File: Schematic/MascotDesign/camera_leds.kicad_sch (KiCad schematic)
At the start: 11 parts, among them Q1 IRF540N

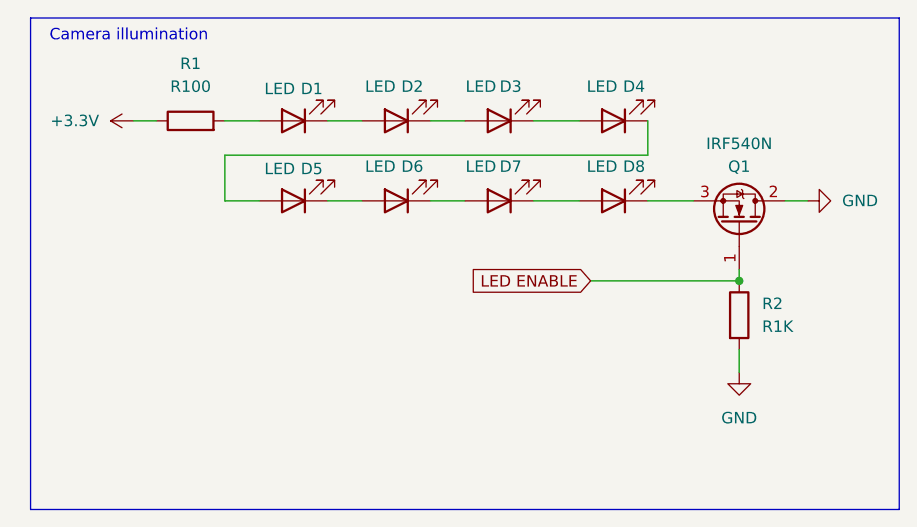
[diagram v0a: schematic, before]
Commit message: Assign footprints and begin PCB layout
Need to check the ECE shop to see what parts we have on hand before we get too far into this, but still.
It's a start.
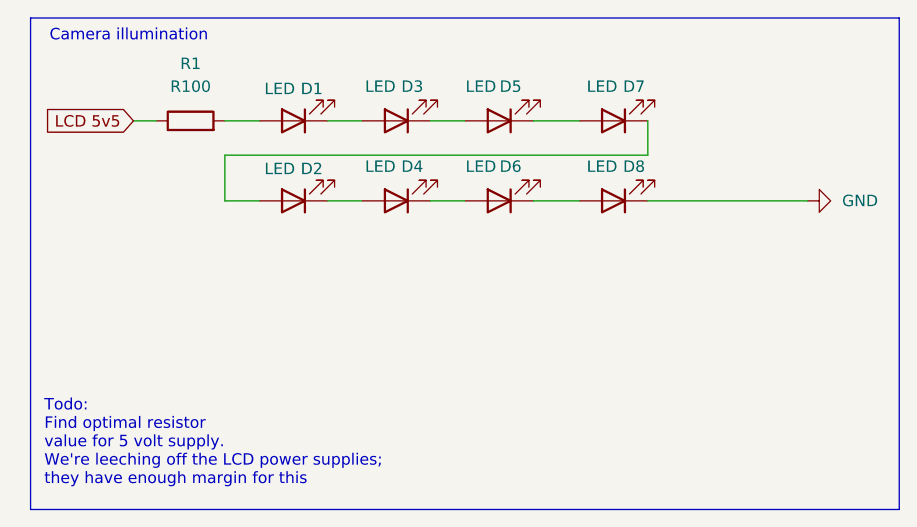
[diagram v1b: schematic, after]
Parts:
- removed Q1: IRF540N, Package_TO_SOT_THT:TO-220-3_Vertical, symbol Transistor_FET:IRF540N
- removed R2: R1K, symbol Device:R
- D1, D8: footprint (none) -> LED_THT:LED_D3.0mm
- D2: renamed from D5; footprint (none) -> LED_THT:LED_D3.0mm
- D3: renamed from D2; footprint (none) -> LED_THT:LED_D3.0mm
- D4: renamed from D6; footprint (none) -> LED_THT:LED_D3.0mm
- D5: renamed from D3; footprint (none) -> LED_THT:LED_D3.0mm
- D6: renamed from D7; footprint (none) -> LED_THT:LED_D3.0mm
- D7: renamed from D4; footprint (none) -> LED_THT:LED_D3.0mm
- R1: footprint (none) -> Resistor_THT:R_Axial_DIN0207_L6.3mm_D2.5mm_P7.62mm_Horizontal
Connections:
- net GND: now also D8.1 (K)
- net +3.3V renamed LCD 5v5
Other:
- note added: "Todo: Find optimal resistor value for 5 volt supply. We're leeching off the LCD power supplies; they have enough margin for this"
- title: (none) -> Camera Light subsystem

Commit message: Work on CAD and schematics
Got most of the components modeled for reference, now arranging them and creating brackets
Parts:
- added J7: LED Connector, Connector_PinHeader_2.54mm:PinHeader_1x02_P2.54mm_Vertical, symbol Connector_Generic:Conn_01x02
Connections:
- net GND: now also J7.2 (Pin_2)
- net LCD 5v5: now also J7.1 (Pin_1)
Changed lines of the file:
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@@
+	(wire
+		(pts
+			(xy 38.1 48.26) (xy 34.29 48.26)
+		)
+		(stroke
+			(width 0)
+			(type default)
+		)
+	)
 	(wire
 		(pts
 			(xy 31.75 27.94) (xy 34.29 27.94)
+		)
+		(stroke
+			(width 0)
+			(type default)
+		)
+	)
+	(wire
+		(pts
+			(xy 38.1 50.8) (xy 34.29 50.8)
 		)
 		(stroke
@@
 		)
 	)
+	(global_label "LCD 5v5"
+		(shape input)
+		(at 34.29 48.26 180)
+		(fields_autoplaced yes)
+		(effects
+			(font
+				(size 1.27 1.27)
+			)
+			(justify right)
+		)
+		(property "Intersheetrefs" "${INTERSHEET_REFS}"
+			(at 23.3825 48.26 0)
+			(effects
+				(font
+					(size 1.27 1.27)
+				)
+				(justify right)
+				(hide yes)
+			)
+		)
+	)
 	(symbol
 		(lib_id "Device:LED")
@@
 	(symbol
 		(lib_id "power:GND")
+		(at 34.29 50.8 270)
+		(unit 1)
+		(exclude_from_sim no)
+		(in_bom yes)
+		(on_board yes)
+		(dnp no)
+		(fields_autoplaced yes)
+		(property "Reference" "#PWR01"
+			(at 27.94 50.8 0)
+			(effects
+				(font
+					(size 1.27 1.27)
+				)
+				(hide yes)
+			)
+		)
+		(property "Value" "GND"
+			(at 30.48 50.7999 90)
+			(effects
+				(font
+					(size 1.27 1.27)
+				)
+				(justify right)
+			)
+		)
+		(property "Footprint" ""
+			(at 34.29 50.8 0)
+			(effects
+				(font
+					(size 1.27 1.27)
+				)
+				(hide yes)
+			)
+		)
+		(property "Datasheet" ""
+			(at 34.29 50.8 0)
+			(effects
+				(font
+					(size 1.27 1.27)
+				)
+				(hide yes)
+			)
+		)
+		(property "Description" "Power symbol creates a global label with name \"GND\" , ground"
+			(at 34.29 50.8 0)
+			(effects
+				(font
+					(size 1.27 1.27)
+				)
+				(hide yes)
+			)
+		)
+		(pin "1"
+		)
+		(instances
+			(project "MascotDesign"
+				(path "/ba045f6c-d730-41b1-992e-d77c9aee61c5/8b76e1c7-16fb-41f9-a46d-90890acff3e2"
+					(reference "#PWR01")
+					(unit 1)
+				)
+			)
+		)
+	)
+	(symbol
+		(lib_id "power:GND")
 		(at 106.68 36.83 90)
 		(unit 1)
@@
 					(unit 1)
 				)
+			)
+		)
+	)
+	(symbol
+		(lib_id "Connector_Generic:Conn_01x02")
+		(at 43.18 48.26 0)
+		(unit 1)
+		(exclude_from_sim no)
+		(in_bom yes)
+		(on_board yes)
+		(dnp no)
+		(property "Reference" "J7"
+			(at 43.18 43.434 0)
+			(effects
+				(font
+					(size 1.27 1.27)
+				)
+				(justify right)
+			)
+		)
+		(property "Value" "LED Connector"
+			(at 43.18 45.212 0)
+			(effects
+				(font
+					(size 1.27 1.27)
+				)
+				(justify right)
+			)
+		)
+		(property "Footprint" "Connector_PinHeader_2.54mm:PinHeader_1x02_P2.54mm_Vertical"
+			(at 43.18 48.26 0)
+			(effects
+				(font
+					(size 1.27 1.27)
+				)
+				(hide yes)
+			)
+		)
+		(property "Datasheet" "~"
+			(at 43.18 48.26 0)
+			(effects
+				(font
+					(size 1.27 1.27)
+				)
+				(hide yes)
+			)
+		)
+		(property "Description" "Generic connector, single row, 01x02, script generated (kicad-library-utils/schlib/autogen/connector/)"
+			(at 43.18 48.26 0)
+			(effects
+				(font
+					(size 1.27 1.27)
+				)
+				(hide yes)
+			)
+		)
+		(pin "2"
+		)
+		(pin "1"
+		)
+		(instances
+			(project "MascotDesign"
+				(path "/ba045f6c-d730-41b1-992e-d77c9aee61c5/8b76e1c7-16fb-41f9-a46d-90890acff3e2"
+					(reference "J7")
+					(unit 1)
+				)

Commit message: Do PCB layout
I need to check our cap footprints to make sure we got the right ones.
Other than that, the PCB should be mostly routed.
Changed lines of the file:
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@@
 		)
+	)
+	(junction
+		(at 36.83 50.8)
+		(diameter 0)
+		(color 0 0 0 0)
 	)
 	(wire
@@
 	(wire
 		(pts
-			(xy 38.1 50.8) (xy 34.29 50.8)
+			(xy 38.1 50.8) (xy 36.83 50.8)
 		)
 		(stroke
@@
 		(pts
 			(xy 76.2 27.94) (xy 81.28 27.94)
+		)
+		(stroke
+			(width 0)
+			(type default)
+		)
+	)
+	(wire
+		(pts
+			(xy 36.83 50.8) (xy 34.29 50.8)
 		)
 		(stroke
@@
 					(unit 1)
 				)
+			)
+		)
+	)
+	(symbol
+		(lib_id "power:PWR_FLAG")
+		(at 36.83 50.8 180)
+		(unit 1)
+		(exclude_from_sim no)
+		(in_bom yes)
+		(on_board yes)
+		(dnp no)
+		(property "Reference" "#FLG04"
+			(at 36.83 52.705 0)
+			(effects
+				(font
+					(size 1.27 1.27)
+				)
+				(hide yes)
+			)
+		)
+		(property "Value" "PWR_FLAG"
+			(at 32.766 55.372 0)
+			(effects
+				(font
+					(size 1.27 1.27)
+				)
+			)
+		)
+		(property "Footprint" ""
+			(at 36.83 50.8 0)
+			(effects
+				(font
+					(size 1.27 1.27)
+				)
+				(hide yes)
+			)
+		)
+		(property "Datasheet" "~"
+			(at 36.83 50.8 0)
+			(effects
+				(font
+					(size 1.27 1.27)
+				)
+				(hide yes)
+			)
+		)
+		(property "Description" "Special symbol for telling ERC where power comes from"
+			(at 36.83 50.8 0)
+			(effects
+				(font
+					(size 1.27 1.27)
+				)
+				(hide yes)
+			)
+		)
+		(pin "1"
+		)
+		(instances
+			(project "MascotDesign"
+				(path "/ba045f6c-d730-41b1-992e-d77c9aee61c5/8b76e1c7-16fb-41f9-a46d-90890acff3e2"
+					(reference "#FLG04")
+					(unit 1)
+				)

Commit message: update PCB and mounting brackets
give PCB the correct footprints for the parts we have and add more mounting brackets for the 3D model
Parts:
- removed J7: LED Connector, Connector_PinHeader_2.54mm:PinHeader_1x02_P2.54mm_Vertical, symbol Connector_Generic:Conn_01x02

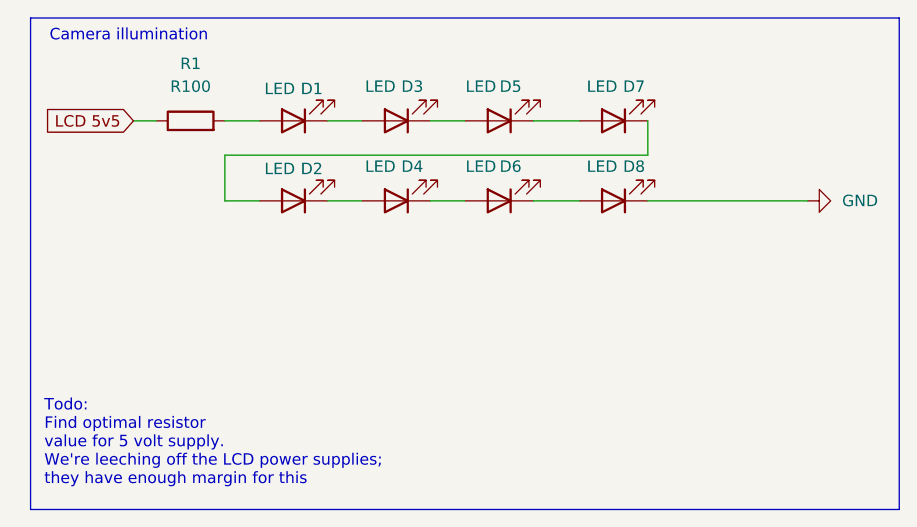
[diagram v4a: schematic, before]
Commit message: Work on CAD and export head + hat slices
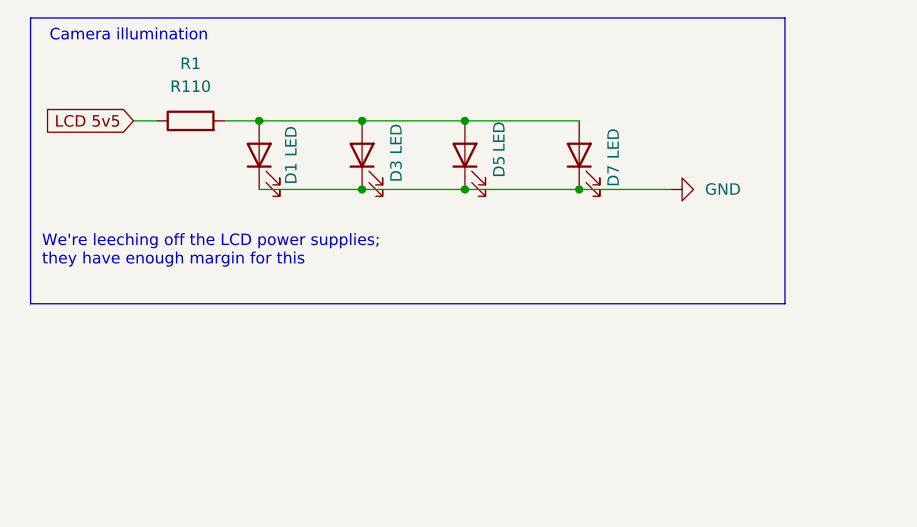
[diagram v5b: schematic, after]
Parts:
- removed D2, D4, D6, D8: LED, LED_THT:LED_D3.0mm, symbol Device:LED
- R1: value R100 -> R110
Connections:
- net GND: now also D1.1 (K), D3.1 (K), D5.1 (K), D7.1 (K)
- net at D5.2 (A): now also D1.2 (A), D3.2 (A), D7.2 (A), R1.2; no longer D3.1 (K)
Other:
- note added: "We're leeching off the LCD power supplies; they have enough margin for this"
- note removed: "Todo: Find optimal resistor value for 5 volt supply. We're leeching off the LCD power supplies; they have enough margin for this"
- moved on the sheet: D1, D3, D5, D7
